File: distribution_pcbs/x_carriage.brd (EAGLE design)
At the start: 60 x 65 mm, 9 parts

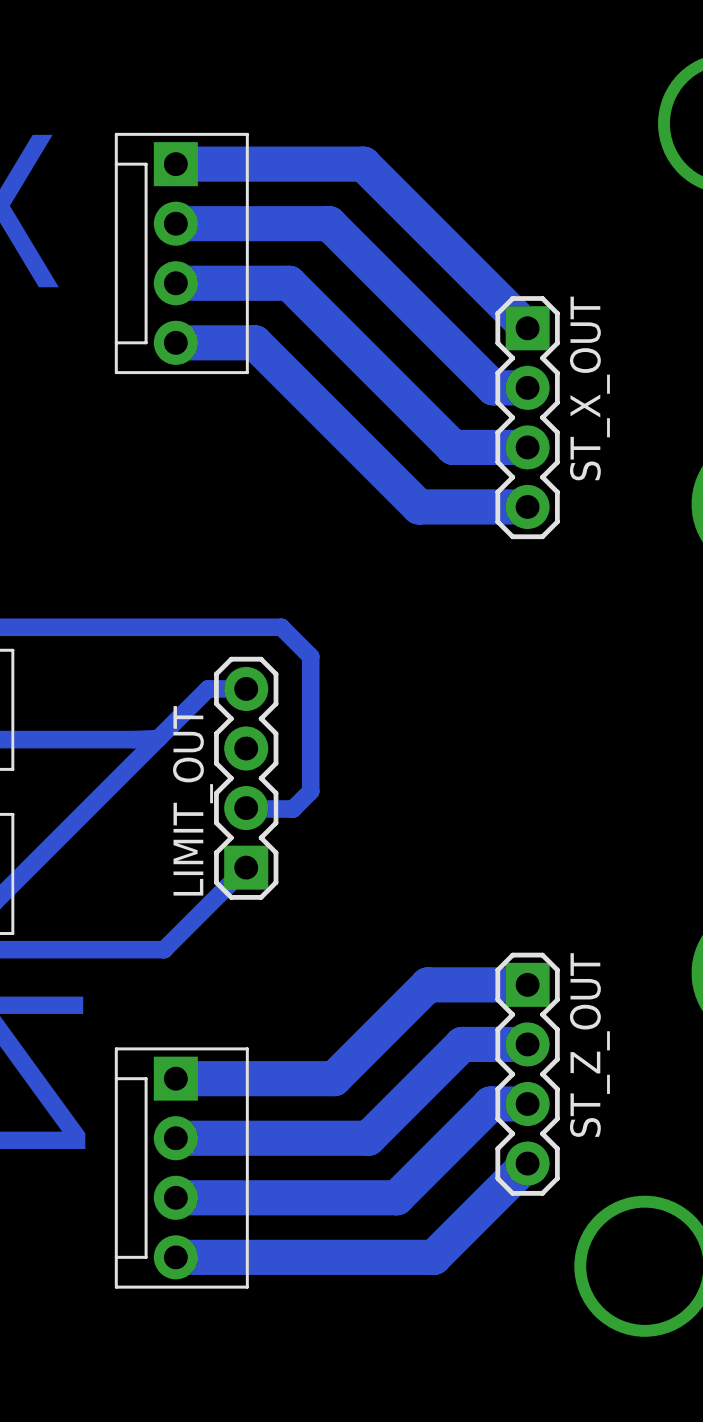
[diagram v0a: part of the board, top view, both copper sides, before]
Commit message: change widths and board dimensions
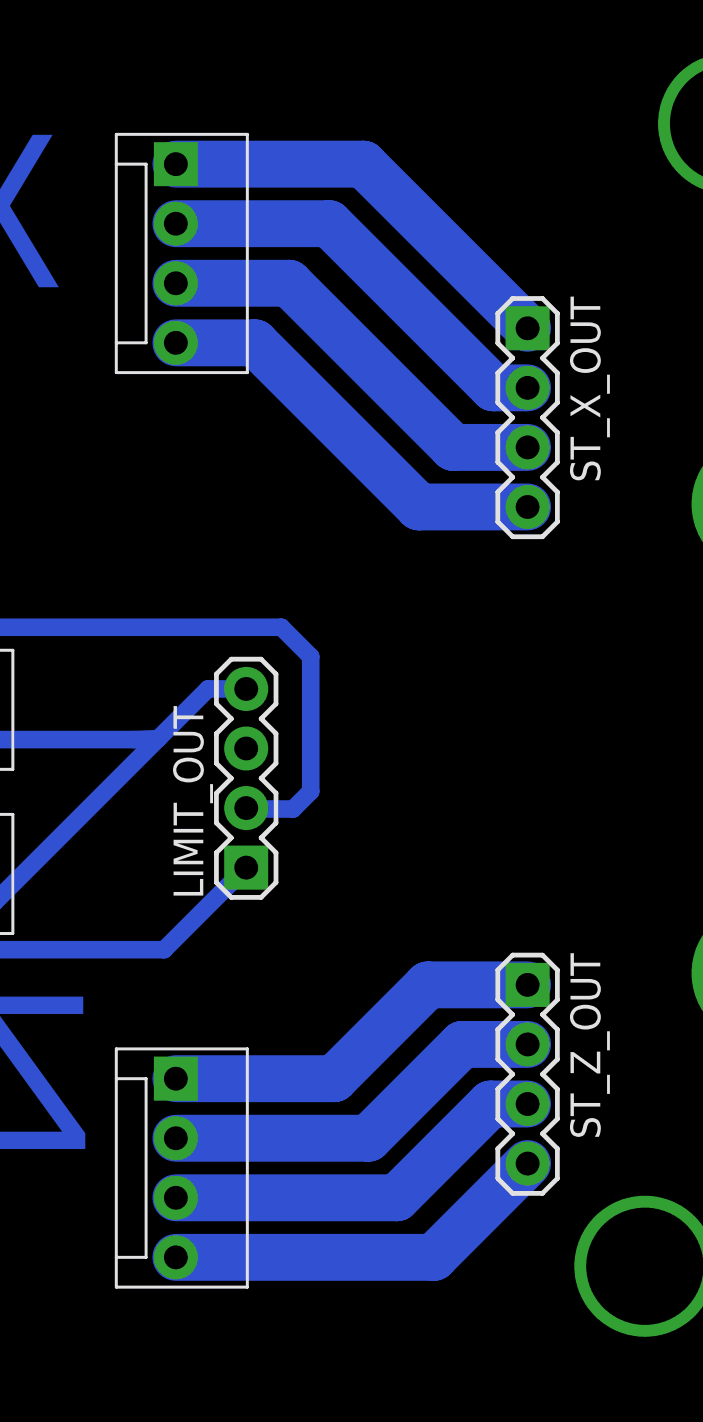
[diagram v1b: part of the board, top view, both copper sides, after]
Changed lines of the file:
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@@
 <?xml version="1.0" encoding="utf-8"?>
 <!DOCTYPE eagle SYSTEM "eagle.dtd">
-<eagle version="7.1.0">
+<eagle version="7.2.0">
 <drawing>
 <settings>
@@
 <param name="mtCopper" value="0.035mm 0.035mm 0.035mm 0.035mm 0.035mm 0.035mm 0.035mm 0.035mm 0.035mm 0.035mm 0.035mm 0.035mm 0.035mm 0.035mm 0.035mm 0.035mm"/>
 <param name="mtIsolate" value="1.5mm 0.15mm 0.2mm 0.15mm 0.2mm 0.15mm 0.2mm 0.15mm 0.2mm 0.15mm 0.2mm 0.15mm 0.2mm 0.15mm 0.2mm"/>
-<param name="mdWireWire" value="16mil"/>
-<param name="mdWirePad" value="16mil"/>
-<param name="mdWireVia" value="16mil"/>
-<param name="mdPadPad" value="16mil"/>
-<param name="mdPadVia" value="16mil"/>
-<param name="mdViaVia" value="16mil"/>
-<param name="mdSmdPad" value="16mil"/>
-<param name="mdSmdVia" value="16mil"/>
-<param name="mdSmdSmd" value="16mil"/>
+<param name="mdWireWire" value="10mil"/>
+<param name="mdWirePad" value="10mil"/>
+<param name="mdWireVia" value="10mil"/>
+<param name="mdPadPad" value="10mil"/>
+<param name="mdPadVia" value="10mil"/>
+<param name="mdViaVia" value="10mil"/>
+<param name="mdSmdPad" value="10mil"/>
+<param name="mdSmdVia" value="10mil"/>
+<param name="mdSmdSmd" value="10mil"/>
 <param name="mdViaViaSameLayer" value="8mil"/>
 <param name="mnLayersViaInSmd" value="2"/>
-<param name="mdCopperDimension" value="40mil"/>
+<param name="mdCopperDimension" value="20mil"/>
 <param name="mdDrill" value="8mil"/>
 <param name="mdSmdStop" value="0mil"/>
@@
 <contactref element="ST_X_IN" pad="4"/>
 <contactref element="ST_X_OUT" pad="4"/>
-<wire x1="30" y1="49.38" x2="33.37" y2="49.38" width="1.5" layer="16"/>
-<wire x1="33.37" y1="49.38" x2="40.37" y2="42.38" width="1.5" layer="16"/>
-<wire x1="40.37" y1="42.38" x2="45" y2="42.38" width="1.5" layer="16"/>
+<wire x1="30" y1="49.38" x2="33.37" y2="49.38" width="2" layer="16"/>
+<wire x1="33.37" y1="49.38" x2="40.37" y2="42.38" width="2" layer="16"/>
+<wire x1="40.37" y1="42.38" x2="45" y2="42.38" width="2" layer="16"/>
 </signal>
 <signal name="N$2">
 <contactref element="ST_X_IN" pad="3"/>
 <contactref element="ST_X_OUT" pad="3"/>
-<wire x1="30" y1="51.92" x2="34.83" y2="51.92" width="1.5" layer="16"/>
-<wire x1="34.83" y1="51.92" x2="41.83" y2="44.92" width="1.5" layer="16"/>
-<wire x1="41.83" y1="44.92" x2="45" y2="44.92" width="1.5" layer="16"/>
+<wire x1="30" y1="51.92" x2="34.83" y2="51.92" width="2" layer="16"/>
+<wire x1="34.83" y1="51.92" x2="41.83" y2="44.92" width="2" layer="16"/>
+<wire x1="41.83" y1="44.92" x2="45" y2="44.92" width="2" layer="16"/>
 </signal>
 <signal name="N$3">
 <contactref element="ST_X_IN" pad="2"/>
 <contactref element="ST_X_OUT" pad="2"/>
-<wire x1="30" y1="54.46" x2="36.54" y2="54.46" width="1.5" layer="16"/>
-<wire x1="36.54" y1="54.46" x2="43.54" y2="47.46" width="1.5" layer="16"/>
-<wire x1="43.54" y1="47.46" x2="45" y2="47.46" width="1.5" layer="16"/>
+<wire x1="30" y1="54.46" x2="36.54" y2="54.46" width="2" layer="16"/>
+<wire x1="36.54" y1="54.46" x2="43.54" y2="47.46" width="2" layer="16"/>
+<wire x1="43.54" y1="47.46" x2="45" y2="47.46" width="2" layer="16"/>
 </signal>
 <signal name="N$4">
 <contactref element="ST_X_IN" pad="1"/>
 <contactref element="ST_X_OUT" pad="1"/>
-<wire x1="30" y1="57" x2="38" y2="57" width="1.5" layer="16"/>
-<wire x1="38" y1="57" x2="45" y2="50" width="1.5" layer="16"/>
+<wire x1="30" y1="57" x2="38" y2="57" width="2" layer="16"/>
+<wire x1="38" y1="57" x2="45" y2="50" width="2" layer="16"/>
 </signal>
 <signal name="N$13">
 <contactref element="ST_Z_IN" pad="4"/>
 <contactref element="ST_Z_OUT" pad="4"/>
-<wire x1="30" y1="10.38" x2="41" y2="10.38" width="1.5" layer="16"/>
-<wire x1="41" y1="10.38" x2="45" y2="14.38" width="1.5" layer="16"/>
+<wire x1="30" y1="10.38" x2="41" y2="10.38" width="2" layer="16"/>
+<wire x1="41" y1="10.38" x2="45" y2="14.38" width="2" layer="16"/>
 </signal>
 <signal name="N$14">
 <contactref element="ST_Z_IN" pad="3"/>
 <contactref element="ST_Z_OUT" pad="3"/>
-<wire x1="30" y1="12.92" x2="39.42" y2="12.92" width="1.5" layer="16"/>
-<wire x1="39.42" y1="12.92" x2="43.42" y2="16.92" width="1.5" layer="16"/>
-<wire x1="43.42" y1="16.92" x2="45" y2="16.92" width="1.5" layer="16"/>
+<wire x1="30" y1="12.92" x2="39.42" y2="12.92" width="2" layer="16"/>
+<wire x1="39.42" y1="12.92" x2="43.42" y2="16.92" width="2" layer="16"/>
+<wire x1="43.42" y1="16.92" x2="45" y2="16.92" width="2" layer="16"/>
 </signal>
 <signal name="N$15">
 <contactref element="ST_Z_IN" pad="2"/>
 <contactref element="ST_Z_OUT" pad="2"/>
-<wire x1="30" y1="15.46" x2="38.21" y2="15.46" width="1.5" layer="16"/>
-<wire x1="38.21" y1="15.46" x2="42.21" y2="19.46" width="1.5" layer="16"/>
-<wire x1="42.21" y1="19.46" x2="45" y2="19.46" width="1.5" layer="16"/>
+<wire x1="30" y1="15.46" x2="38.21" y2="15.46" width="2" layer="16"/>
+<wire x1="38.21" y1="15.46" x2="42.21" y2="19.46" width="2" layer="16"/>
+<wire x1="42.21" y1="19.46" x2="45" y2="19.46" width="2" layer="16"/>
 </signal>
 <signal name="N$16">
 <contactref element="ST_Z_IN" pad="1"/>
 <contactref element="ST_Z_OUT" pad="1"/>
-<wire x1="30" y1="18" x2="36.75" y2="18" width="1.5" layer="16"/>
-<wire x1="36.75" y1="18" x2="40.75" y2="22" width="1.5" layer="16"/>
-<wire x1="40.75" y1="22" x2="45" y2="22" width="1.5" layer="16"/>
+<wire x1="30" y1="18" x2="36.75" y2="18" width="2" layer="16"/>
+<wire x1="36.75" y1="18" x2="40.75" y2="22" width="2" layer="16"/>
+<wire x1="40.75" y1="22" x2="45" y2="22" width="2" layer="16"/>
 </signal>
 <signal name="GNDA">
